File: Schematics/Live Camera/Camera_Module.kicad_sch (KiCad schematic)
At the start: 91 parts, among them J1 Stack Male Edge Connector, J2 SWD_01x04_Pin, J4 Therm_In, J4 USB_C_Female_USB2_Small, J5 VTX_DAT, J6 RunCam6, J8 VTX_PWR, Q3 AO3400A, Q3 AO3401A, Q4 AO3400A, Q5 AO3401A, SW1 SW_STM_RESET, SW2 SW_STM_BOOT_MODE, U1 CP2102N-Axx-xQFN28, U1 LM66100DCKR, U1 STM32F103CBT6, U12 AMS1117-3.3, U3 W25Q128JVS, U5 LM66100DCKR, U6 LM66100DCKR, U8 ISO1042BDWVR, Y1 X322516MMB4SI

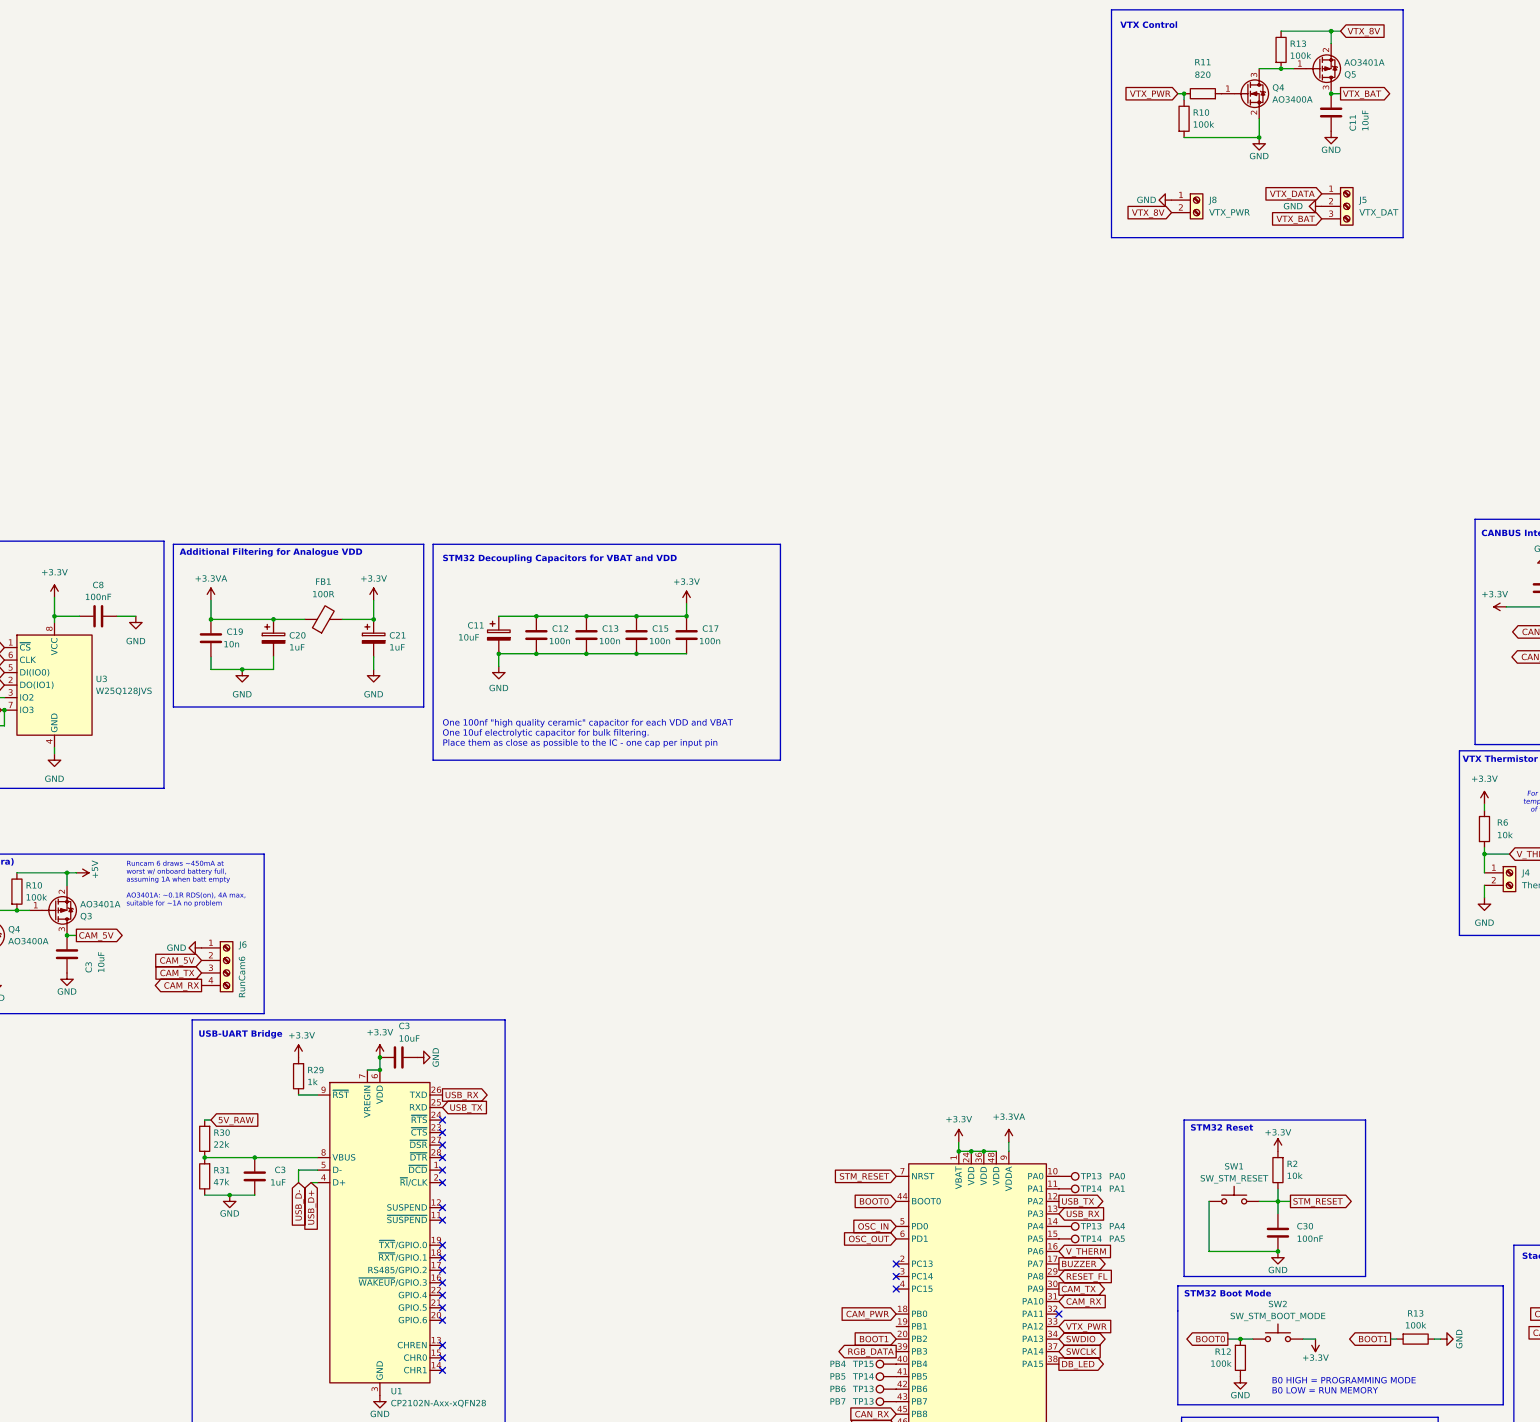
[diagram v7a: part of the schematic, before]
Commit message: Added battery frontend for VTX
Added battery + switch connectors, reverse polarity protection, and battery voltage sense circuit. Adjusted existing VTX connector to now only handle GND/V+/Data.
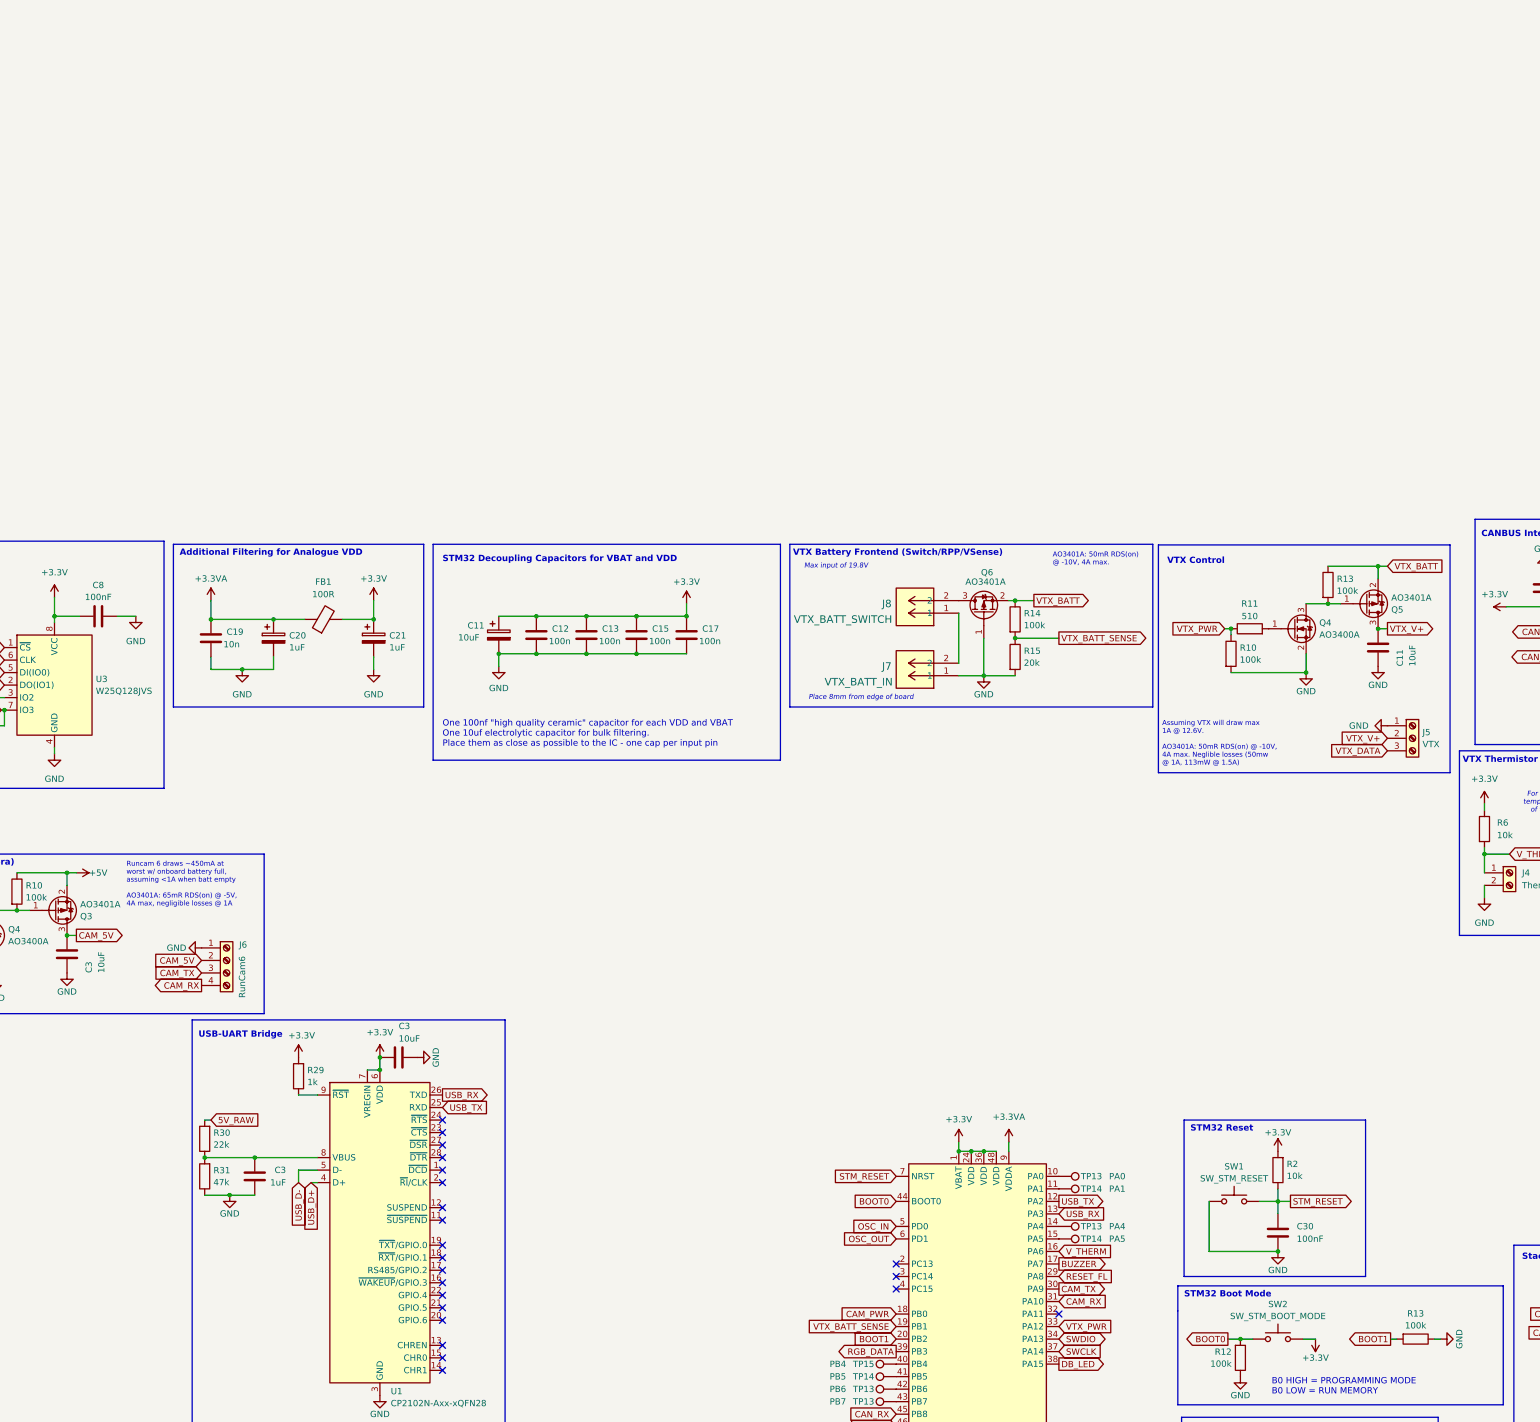
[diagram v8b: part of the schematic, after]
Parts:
- removed J8: VTX_PWR, TerminalBlock_TE-Connectivity:TerminalBlock_TE_282834-2_1x02_P2.54mm_Horizontal, symbol Connector:Screw_Terminal_01x02
- added J7: VTX_BATT_IN, footprints:CONN_2-1445057-2_TYCO, symbol CONN_2-1445057-2_TYCO:2-1445057-2
- added J8: VTX_BATT_SWITCH, footprints:CONN_2-1445057-2_TYCO, symbol CONN_2-1445057-2_TYCO:2-1445057-2
- added Q6: AO3401A, Package_TO_SOT_SMD:SOT-23, symbol Transistor_FET:AO3401A
- added R14: 100k, Resistor_SMD:R_0603_1608Metric, symbol Device:R
- added R15: 20k, Resistor_SMD:R_0603_1608Metric, symbol Device:R
- J5: value VTX_DAT -> VTX
- R11: value 820 -> 510
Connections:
- net GND: now also J5.1 (Pin_1), J7.1, Q6.1 (G), R15.2; no longer J5.2 (Pin_2)
- net VTX_DATA: now also J5.3 (Pin_3); no longer J5.1 (Pin_1)
- net VTX_BATT_SENSE: now reaches U1.19 (PB1)
- net VTX_BATT_SENSE: now also R14.2, R15.1
- net VTX_8V renamed VTX_BATT
- net VTX_BATT: now also Q6.2 (S), R14.1
- net VTX_BAT renamed VTX_V+
- net VTX_V+: now also J5.2 (Pin_2); no longer J5.3 (Pin_3)
- new net: J7.2, J8.1
- new net: J8.2, Q6.3 (D)
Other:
- note added: "AO3401A: 50mR RDS(on) @ -10V, 4A max."
- note added: "Assuming VTX will draw max 1A @ 12.6V. AO3401A: 50mR RDS(on) @ -10V, 4A max. Neglible losses (50mw @ 1A, 113mW @ 1.5A)"
- note added: "Max input of 19.8V"
- note added: "Place 8mm from edge of board"
- note added: "Runcam 6 draws ~450mA at worst w/ onboard battery full, assuming <1A when batt empty AO3401A: 65mR RDS(on) @ -5V, 4A max, negligible losses @ 1A"
- note added: "VTX Battery Frontend (Switch/RPP/VSense)"
- note removed: "Runcam 6 draws ~450mA at worst w/ onboard battery full, assuming 1A when batt empty AO3401A: ~0.1R RDS(on), 4A max, suitable for ~1A no problem"
- moved on the sheet: C11, J5, Q4, Q5, R10, R11, R13
